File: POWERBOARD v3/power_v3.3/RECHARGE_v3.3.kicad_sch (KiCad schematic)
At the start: 27 parts, among them J1 B2B_PH_K_S, J2 USB_C_Receptacle_USB2.0_16P, J3 R14 - 103AT-2, U1 USBLC6-2, U2 BQ25886RGE

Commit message: added footprints
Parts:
- removed CHAR/BATT1: CHAR/BATT, Connector_PinHeader_2.00mm:PinHeader_1x02_P2.00mm_Vertical, symbol Connector_Generic:Conn_01x02
- removed J1: B2B_PH_K_S, Connector_JST:JST_PH_B2B-PH-K_1x02_P2.00mm_Vertical, symbol Connector_Generic:Conn_01x02
- removed J2: USB_C_Receptacle_USB2.0_16P, symbol Connector:USB_C_Receptacle_USB2.0_16P
- removed J3: R14 - 103AT-2, symbol Connector_Generic:Conn_01x02
- added BAT1: TestPoint, TestPoint:TestPoint_Keystone_5000-5004_Miniature, symbol Connector:TestPoint
- added C13: 22n, Capacitor_SMD:C_0201_0603Metric, symbol Device:C
- added J1: 2053380003, footprintsusbc:CONN_2053380000-SD_03_MOL, symbol 2026-10-06_11-57-55:2053380003
- added J2: UJ20-C-H-G-SMT-1-P16-TR, UJ20-C-H-G-SMT-1-P16-TR:SAMESKY_UJ20-C-H-G-SMT-1-P16-TR, symbol UJ20-C-H-G-SMT-1-P16-TR:UJ20-C-H-G-SMT-1-P16-TR
- C1: value 30u -> 22u
- C2: value 47n -> 22n; footprint Capacitor_SMD:C_1206_3216Metric -> Capacitor_SMD:C_0201_0603Metric
- C4, C8, C9: footprint (none) -> Capacitor_SMD:C_1206_3216Metric
- C6, C7: footprint Capacitor_SMD:C_0805_2012Metric -> Capacitor_SMD:C_1206_3216Metric
- D1, D2: footprint LED_SMD:LED_0805_2012Metric -> LED_SMD:LED_0603_1608Metric
- L1: footprint (none) -> 74438336010:INDC3030X200N
- R1: value 3.9k -> 6.2k; footprint Resistor_SMD:R_0805_2012Metric -> Resistor_SMD:R_0603_1608Metric
- R2, R4, R6, R7, R8, R9: footprint Resistor_SMD:R_0805_2012Metric -> Resistor_SMD:R_0603_1608Metric
- R3, R5: footprint (none) -> Resistor_SMD:R_0603_1608Metric
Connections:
- net BATTERY VOLTAGE: now also C8.1, U2.13 (BAT), U2.14 (BAT), BAT1.1, J1.3
- net BTST: now also C13.2
- net CC1: now also J2.A5 (CC1)
- net CC2: now also J2.B5 (CC2)
- net GND: now also J1.1, J2.A1_B12 (GND), J2.B1_A12 (GND__1), J2.SH1 (SHIELD), J2.SH2 (SHIELD__1), J2.SH3 (SHIELD__2), J2.SH4 (SHIELD__3); no longer U1.2 (GND)
- net SW: now also C13.1
- net VBUS: now also J2.A4_B9 (VBUS), J2.B4_A9 (VBUS__1)
- net at U1.1 (I/O1): now also J2.A6 (DP1), J2.B6 (DP2)
- net at U1.3 (I/O2): now also J2.A7 (DN1), J2.B7 (DN2)
- net TS renamed NTC
- net NTC: now also J1.2
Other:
- moved on the sheet: C2, C8, C9, D1, D2, R6, R7, R8, R9, U1, U2

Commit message: finished footprint assignment, added on-off general switch
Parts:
- J2: footprint UJ20-C-H-G-SMT-1-P16-TR:SAMESKY_UJ20-C-H-G-SMT-1-P16-TR -> UJ20_C_H_G_SMT_1_P16_TR:SAMESKY_UJ20-C-H-G-SMT-1-P16-TR
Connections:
- net GND: now also U1.2 (GND)
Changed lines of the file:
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@@
+	(wire
+		(pts
+			(xy 67.31 185.42) (xy 77.47 185.42)
+		)
+		(stroke
+			(width 0)
+			(type default)
+		)
+	)
 	(wire
 		(pts
@@
 	(wire
 		(pts
+			(xy 77.47 151.13) (xy 77.47 185.42)
+		)
+		(stroke
+			(width 0)
+			(type default)
+		)
+	)
+	(wire
+		(pts
 			(xy 33.02 43.18) (xy 33.02 36.83)
 		)
@@
 		(pts
 			(xy 59.69 36.83) (xy 52.07 36.83)
-		)
-		(stroke
-			(width 0)
-			(type default)
-		)
-	)
-	(wire
-		(pts
-			(xy 77.47 151.13) (xy 77.47 177.8)
 		)
 		(stroke
@@
 			)
 		)
-		(property "Footprint" "UJ20-C-H-G-SMT-1-P16-TR:SAMESKY_UJ20-C-H-G-SMT-1-P16-TR"
+		(property "Footprint" "UJ20_C_H_G_SMT_1_P16_TR:SAMESKY_UJ20-C-H-G-SMT-1-P16-TR"
 			(at 45.72 152.4 0)
 			(hide yes)

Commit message: (nearly) finished schematic and layout, beginning routing (hooooooly)
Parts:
- removed C9: 22u, Capacitor_SMD:C_1206_3216Metric, symbol Device:C
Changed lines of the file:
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@@
 	)
 	(junction
+		(at 209.55 46.99)
+		(diameter 0)
+		(color 0 0 0 0)
+	)
+	(junction
 		(at 238.76 133.35)
 		(diameter 0)
@@
 	)
 	(junction
-		(at 224.79 119.38)
-		(diameter 0)
-		(color 0 0 0 0)
-	)
-	(junction
 		(at 60.96 147.32)
 		(diameter 0)
@@
 	)
 	(junction
-		(at 209.55 46.99)
-		(diameter 0)
-		(color 0 0 0 0)
-	)
-	(junction
 		(at 67.31 177.8)
 		(diameter 0)
@@
 	(wire
 		(pts
+			(xy 83.82 101.6) (xy 83.82 107.95)
+		)
+		(stroke
+			(width 0)
+			(type default)
+		)
+	)
+	(wire
+		(pts
 			(xy 67.31 177.8) (xy 67.31 180.34)
 		)
@@
 	(wire
 		(pts
-			(xy 209.55 46.99) (xy 217.17 46.99)
+			(xy 33.02 50.8) (xy 33.02 54.61)
 		)
 		(stroke
@@
 	(wire
 		(pts
-			(xy 33.02 50.8) (xy 33.02 54.61)
+			(xy 237.49 107.95) (xy 229.87 107.95)
 		)
 		(stroke
@@
 	(wire
 		(pts
-			(xy 237.49 107.95) (xy 229.87 107.95)
+			(xy 209.55 46.99) (xy 217.17 46.99)
 		)
 		(stroke
@@
 	(wire
 		(pts
-			(xy 213.36 119.38) (xy 213.36 130.81)
-		)
-		(stroke
-			(width 0)
-			(type default)
-		)
-	)
-	(wire
-		(pts
 			(xy 49.53 110.49) (xy 78.74 110.49)
 		)
@@
 	(wire
 		(pts
-			(xy 224.79 119.38) (xy 233.68 119.38)
-		)
-		(stroke
-			(width 0)
-			(type default)
-		)
-	)
-	(wire
-		(pts
 			(xy 81.28 57.15) (xy 91.44 57.15)
 		)
@@
 	(wire
 		(pts
-			(xy 213.36 130.81) (xy 193.04 130.81)
+			(xy 193.04 130.81) (xy 215.9 130.81)
 		)
 		(stroke
@@
 	(wire
 		(pts
-			(xy 49.53 107.95) (xy 78.74 107.95)
-		)
-		(stroke
-			(width 0)
-			(type default)
-		)
-	)
-	(wire
-		(pts
 			(xy 58.42 142.24) (xy 60.96 142.24)
 		)
@@
 	(wire
 		(pts
+			(xy 83.82 107.95) (xy 49.53 107.95)
+		)
+		(stroke
+			(width 0)
+			(type default)
+		)
+	)
+	(wire
+		(pts
 			(xy 60.96 149.86) (xy 60.96 147.32)
 		)
@@
 	(wire
 		(pts
-			(xy 213.36 119.38) (xy 224.79 119.38)
-		)
-		(stroke
-			(width 0)
-			(type default)
-		)
-	)
-	(wire
-		(pts
 			(xy 237.49 101.6) (xy 237.49 104.14)
 		)
@@
 		)
 	)
-	(label "TS"
-		(at 203.2 143.51 180)
-		(effects
-			(font
-				(size 1.27 1.27)
-			)
-			(justify right bottom)
-		)
-	)
 	(label "SW"
 		(at 200.66 120.65 0)
@@
 		)
 	)
-	(label "NTC"
-		(at 78.74 107.95 180)
-		(effects
-			(font
-				(size 1.27 1.27)
-			)
-			(justify right bottom)
-		)
-	)
 	(label "D-"
 		(at 162.56 115.57 0)
@@
 		)
 	)
-	(label "NTC"
-		(at 217.17 46.99 0)
-		(effects
-			(font
-				(size 1.27 1.27)
-			)
-			(justify left bottom)
-		)
-	)
 	(label "ILIM"
 		(at 162.56 143.51 0)
@@
 		)
 	)
-	(label "TS"
+	(global_label "TS"
+		(shape input)
+		(at 203.2 143.51 0)
+		(fields_autoplaced yes)
+		(effects
+			(font
+				(size 1.27 1.27)
+			)
+			(justify left)
+		)
+		(property "Intersheetrefs" "${INTERSHEET_REFS}"
+			(at 208.3623 143.51 0)
+			(hide yes)
+			(show_name no)
+			(do_not_autoplace no)
+			(effects
+				(font
+					(size 1.27 1.27)
+				)
+				(justify left)
+			)
+		)
+	)
+	(global_label "NTC"
+		(shape bidirectional)
+		(at 217.17 46.99 0)
+		(fields_autoplaced yes)
+		(effects
+			(font
+				(size 1.27 1.27)
+			)
+			(justify left)
+		)
+		(property "Intersheetrefs" "${INTERSHEET_REFS}"
+			(at 224.8346 46.99 0)
+			(hide yes)
+			(show_name no)
+			(do_not_autoplace no)
+			(effects
+				(font
+					(size 1.27 1.27)
+				)
+				(justify left)
+			)
+		)
+	)
+	(global_label "TS"
+		(shape input)
 		(at 209.55 44.45 90)
+		(fields_autoplaced yes)
 		(effects
 			(font
 				(size 1.27 1.27)
 			)
-			(justify left bottom)
+			(justify left)
+		)
+		(property "Intersheetrefs" "${INTERSHEET_REFS}"
+			(at 209.55 39.2877 90)
+			(hide yes)
+			(show_name no)
+			(do_not_autoplace no)
+			(effects
+				(font
+					(size 1.27 1.27)
+				)
+				(justify left)
+			)
+		)
+	)
+	(global_label "NTC"
+		(shape bidirectional)
+		(at 83.82 101.6 90)
+		(fields_autoplaced yes)
+		(effects
+			(font
+				(size 1.27 1.27)
+			)
+			(justify left)
+		)
+		(property "Intersheetrefs" "${INTERSHEET_REFS}"
+			(at 83.82 93.9354 90)
+			(hide yes)
+			(show_name no)
+			(do_not_autoplace no)
+			(effects
+				(font
+					(size 1.27 1.27)
+				)
+				(justify left)
+			)
 		)
 	)
 	(hierarchical_label "SYS"
 		(shape output)
-		(at 233.68 119.38 0)
+		(at 215.9 130.81 0)
 		(effects
 			(font
@@
 	)
 	(symbol
-		(lib_id "power:GND")
-		(at 224.79 127 0)
-		(unit 1)
-		(body_style 1)
-		(exclude_from_sim no)
-		(in_bom yes)
-		(on_board yes)
-		(in_pos_files yes)
-		(dnp no)
-		(fields_autoplaced yes)
-		(property "Reference" "#PWR015"
-			(at 224.79 133.35 0)
-			(hide yes)
-			(show_name no)
-			(do_not_autoplace no)
-			(effects
-				(font
-					(size 1.27 1.27)
-				)
-			)
-		)
-		(property "Value" "GND"
-			(at 224.79 132.08 0)
-			(show_name no)
-			(do_not_autoplace no)
-			(effects
-				(font
-					(size 1.27 1.27)
-				)
-			)
-		)
-		(property "Footprint" ""
-			(at 224.79 127 0)
-			(hide yes)
-			(show_name no)
-			(do_not_autoplace no)
-			(effects
-				(font
-					(size 1.27 1.27)
-				)
-			)
-		)
-		(property "Datasheet" ""
-			(at 224.79 127 0)
-			(hide yes)
-			(show_name no)
-			(do_not_autoplace no)
-			(effects
-				(font
-					(size 1.27 1.27)
-				)
-			)
-		)
-		(property "Description" "Power symbol creates a global label with name \"GND\" , ground"
-			(at 224.79 127 0)
-			(hide yes)
-			(show_name no)
-			(do_not_autoplace no)
-			(effects
-				(font
-					(size 1.27 1.27)
-				)
-			)
-		)
-		(pin "1"
-		)
-		(instances
-			(project "power_v3.3"
-				(path "/432bcdcf-747a-4fa0-b87b-096f44260199/ef6b3a2b-31e3-4ffb-9457-e6034dbdb4b5"
-					(reference "#PWR015")
-					(unit 1)
-				)
-			)
-		)
-	)
-	(symbol
 		(lib_id "Device:C")
 		(at 54.61 59.69 0)
@@
 					(unit 1)
 				)
-			)
-		)
-	)
-	(symbol
-		(lib_id "Device:C")
-		(at 224.79 123.19 0)
-		(unit 1)
-		(body_style 1)
-		(exclude_from_sim no)
-		(in_bom yes)
-		(on_board yes)
-		(in_pos_files yes)
-		(dnp no)
-		(fields_autoplaced yes)
-		(property "Reference" "C9"
-			(at 228.6 121.9199 0)
-			(show_name no)
-			(do_not_autoplace no)
-			(effects
-				(font
-					(size 1.27 1.27)
-				)
-				(justify left)
-			)
-		)
-		(property "Value" "22u"
-			(at 228.6 124.4599 0)
-			(show_name no)
-			(do_not_autoplace no)
-			(effects
-				(font
-					(size 1.27 1.27)
-				)
-				(justify left)
-			)
-		)
-		(property "Footprint" "Capacitor_SMD:C_1206_3216Metric"
-			(at 225.7552 127 0)
-			(hide yes)
-			(show_name no)
-			(do_not_autoplace no)
-			(effects
-				(font
-					(size 1.27 1.27)
-				)
-			)
-		)
-		(property "Datasheet" ""
-			(at 224.79 123.19 0)
-			(hide yes)
-			(show_name no)
-			(do_not_autoplace no)
-			(effects
-				(font
-					(size 1.27 1.27)
-				)
-			)
-		)
-		(property "Description" "Unpolarized capacitor"
-			(at 224.79 123.19 0)
-			(hide yes)
-			(show_name no)
-			(do_not_autoplace no)
-			(effects
-				(font
-					(size 1.27 1.27)
-				)
-			)
-		)
-		(pin "1"
-		)
-		(pin "2"
-		)
-		(instances
-			(project "power_v3.3"
-				(path "/432bcdcf-747a-4fa0-b87b-096f44260199/ef6b3a2b-31e3-4ffb-9457-e6034dbdb4b5"
-					(reference "C9")
-					(unit 1)
-				)

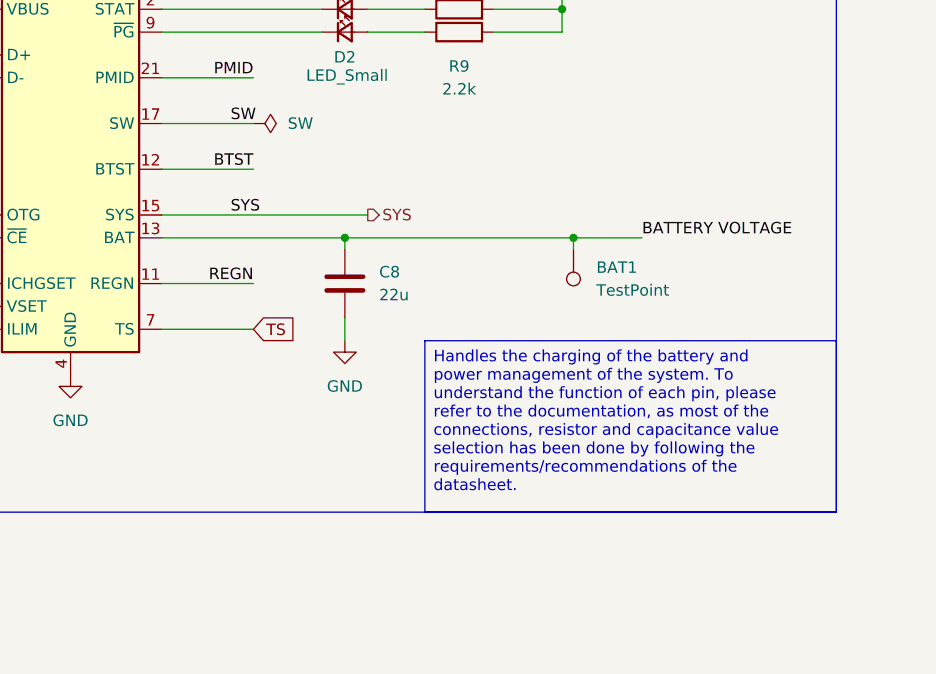
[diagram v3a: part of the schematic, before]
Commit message: updated routing, added mounting holes
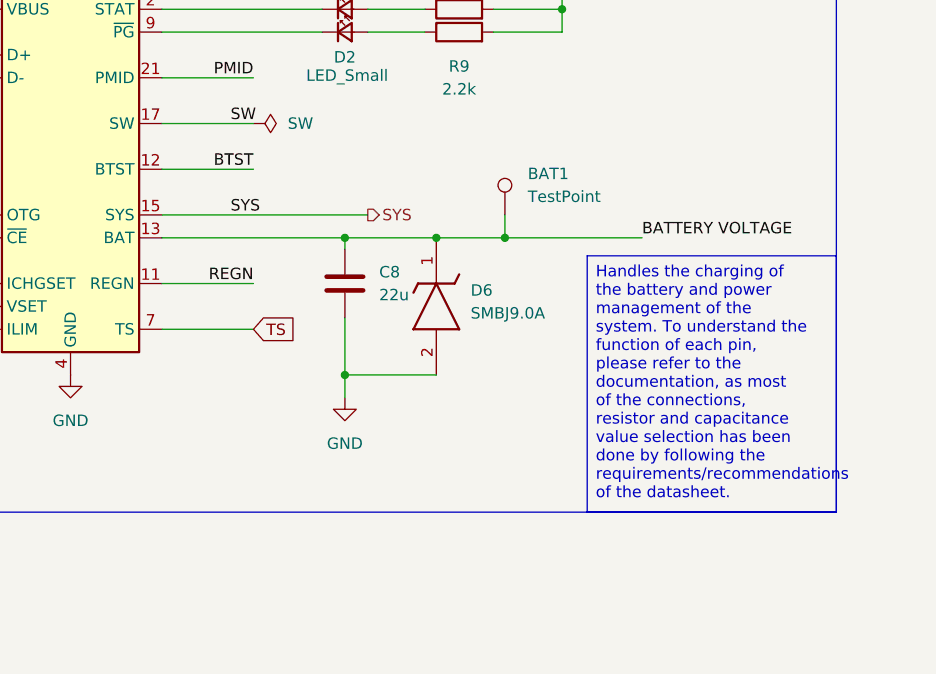
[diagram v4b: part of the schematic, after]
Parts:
- added D6: SMBJ9.0A, SMBJ9.0A:DIOM5436X261N, symbol SMBJ9_0A:SMBJ9.0A
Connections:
- net BATTERY VOLTAGE: now also D6.1 (K)
- net GND: now also D6.2 (A)
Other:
- moved on the sheet: BAT1
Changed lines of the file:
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@@
 	(text_box "Handles the charging of the battery and power management of the system. To understand the function of each pin, please refer to the documentation, as most of the connections, resistor and capacitance value selection has been done by following the requirements/recommendations of the datasheet."
 		(exclude_from_sim no)
-		(at 222.25 144.7799 0)
-		(size 45.72 19.0501)
+		(at 240.284 135.3462 0)
+		(size 27.686 28.4838)
 		(margins 0.9525 0.9525 0.9525 0.9525)
 		(stroke
@@
 	)
 	(junction
-		(at 238.76 133.35)
+		(at 231.14 133.35)
 		(diameter 0)
 		(color 0 0 0 0)
@@
 	)
 	(junction
+		(at 223.52 133.35)
+		(diameter 0)
+		(color 0 0 0 0)
+	)
+	(junction
 		(at 67.31 180.34)
 		(diameter 0)
@@
 	)
 	(junction
+		(at 213.36 148.59)
+		(diameter 0)
+		(color 0 0 0 0)
+	)
+	(junction
 		(at 170.18 44.45)
 		(diameter 0)
@@
 	(wire
 		(pts
+			(xy 213.36 148.59) (xy 213.36 142.24)
+		)
+		(stroke
+			(width 0)
+			(type default)
+		)
+	)
+	(wire
+		(pts
 			(xy 60.96 132.08) (xy 77.47 132.08)
 		)
@@
 	(wire
 		(pts
-			(xy 213.36 144.78) (xy 213.36 142.24)
+			(xy 213.36 151.13) (xy 213.36 148.59)
 		)
 		(stroke
@@
 	(wire
 		(pts
-			(xy 193.04 133.35) (xy 238.76 133.35)
+			(xy 223.52 133.35) (xy 246.38 133.35)
+		)
+		(stroke
+			(width 0)
+			(type default)
+		)
+	)
+	(wire
+		(pts
+			(xy 193.04 133.35) (xy 223.52 133.35)
 		)
 		(stroke
@@
 	(wire
 		(pts
-			(xy 238.76 134.62) (xy 238.76 133.35)
+			(xy 231.14 130.81) (xy 231.14 133.35)
 		)
 		(stroke
@@
 	(wire
 		(pts
-			(xy 213.36 134.62) (xy 213.36 133.35)
+			(xy 213.36 148.59) (xy 223.52 148.59)
 		)
 		(stroke
@@
 	(wire
 		(pts
-			(xy 43.18 64.77) (xy 43.18 63.5)
+			(xy 213.36 134.62) (xy 213.36 133.35)
 		)
 		(stroke
@@
 	(wire
 		(pts
-			(xy 238.76 133.35) (xy 246.38 133.35)
+			(xy 43.18 64.77) (xy 43.18 63.5)
 		)
 		(stroke
@@
 	)
 	(symbol
+		(lib_id "SMBJ9_0A:SMBJ9.0A")
+		(at 223.52 133.35 270)
+		(unit 1)
+		(body_style 1)
+		(exclude_from_sim no)
+		(in_bom yes)
+		(on_board yes)
+		(in_pos_files yes)
+		(dnp no)
+		(fields_autoplaced yes)
+		(property "Reference" "D6"
+			(at 227.33 139.1919 90)
+			(show_name no)
+			(do_not_autoplace no)
+			(effects
+				(font
+					(size 1.27 1.27)
+				)
+				(justify left)
+			)
+		)
+		(property "Value" "SMBJ9.0A"
+			(at 227.33 141.7319 90)
+			(show_name no)
+			(do_not_autoplace no)
+			(effects
+				(font
+					(size 1.27 1.27)
+				)
+				(justify left)
+			)
+		)
+		(property "Footprint" "SMBJ9.0A:DIOM5436X261N"
+			(at 129.87 143.51 0)
+			(hide yes)
+			(show_name no)
+			(do_not_autoplace no)
+			(effects
+				(font
+					(size 1.27 1.27)
+				)
+				(justify left bottom)
+			)
+		)
+		(property "Datasheet" "https://www.semtech.com/products/circuit-protection/esd-protection/smbj9.0a"
+			(at 29.87 143.51 0)
+			(hide yes)
+			(show_name no)
+			(do_not_autoplace no)
+			(effects
+				(font
+					(size 1.27 1.27)
+				)
+				(justify left bottom)
+			)
+		)
+		(property "Description" "1-Line ESD Protection"
+			(at 223.52 133.35 0)
+			(hide yes)
+			(show_name no)
+			(do_not_autoplace no)
+			(effects
+				(font
+					(size 1.27 1.27)
+				)
+			)
+		)
+		(property "Height" "2.61"
+			(at -170.13 143.51 0)
+			(hide yes)
+			(show_name no)
+			(do_not_autoplace no)
+			(effects
+				(font
+					(size 1.27 1.27)
+				)
+				(justify left bottom)
+			)
+		)
+		(property "Mouser Part Number" ""
+			(at -270.13 143.51 0)
+			(hide yes)
+			(show_name no)
+			(do_not_autoplace no)
+			(effects
+				(font
+					(size 1.27 1.27)
+				)
+				(justify left bottom)
+			)
+		)
+		(property "Mouser Price/Stock" ""
+			(at -370.13 143.51 0)
+			(hide yes)
+			(show_name no)
+			(do_not_autoplace no)
+			(effects
+				(font
+					(size 1.27 1.27)
+				)
+				(justify left bottom)
+			)
+		)
+		(property "Manufacturer_Name" "SEMTECH"
+			(at -470.13 143.51 0)
+			(hide yes)
+			(show_name no)
+			(do_not_autoplace no)
+			(effects
+				(font
+					(size 1.27 1.27)
+				)
+				(justify left bottom)
+			)
+		)
+		(property "Manufacturer_Part_Number" "SMBJ9.0A"
+			(at -570.13 143.51 0)
+			(hide yes)
+			(show_name no)
+			(do_not_autoplace no)
+			(effects
+				(font
+					(size 1.27 1.27)
+				)
+				(justify left bottom)
+			)
+		)
+		(pin "1"
+		)
+		(pin "2"
+		)
+		(instances
+			(project "power_v3.3"
+				(path "/432bcdcf-747a-4fa0-b87b-096f44260199/ef6b3a2b-31e3-4ffb-9457-e6034dbdb4b5"
+					(reference "D6")
+					(unit 1)
+				)
+			)
+		)
+	)
+	(symbol
 		(lib_id "power:PWR_FLAG")
 		(at 237.49 104.14 270)
@@
 	(symbol
 		(lib_id "Connector:TestPoint")
-		(at 238.76 134.62 180)
+		(at 231.14 130.81 0)
 		(unit 1)
 		(body_style 1)
@@
 		(fields_autoplaced yes)
 		(property "Reference" "BAT1"
-			(at 241.3 136.6519 0)
+			(at 233.68 126.2379 0)
 			(show_name no)
 			(do_not_autoplace no)
@@
 					(size 1.27 1.27)
 				)
-				(justify right)
+				(justify left)
 			)
 		)
 		(property "Value" "TestPoint"
-			(at 241.3 139.1919 0)
+			(at 233.68 128.7779 0)
 			(show_name no)
 			(do_not_autoplace no)
@@
 					(size 1.27 1.27)
 				)
-				(justify right)
+				(justify left)
 			)
 		)
 		(property "Footprint" "TestPoint:TestPoint_Keystone_5000-5004_Miniature"
-			(at 233.68 134.62 0)
+			(at 236.22 130.81 0)
 			(hide yes)
 			(show_name no)
@@
 		)
 		(property "Datasheet" ""
-			(at 233.68 134.62 0)
+			(at 236.22 130.81 0)
 			(hide yes)
 			(show_name no)
@@
 		)
 		(property "Description" "test point"
-			(at 238.76 134.62 0)
+			(at 231.14 130.81 0)
 			(hide yes)
 			(show_name no)
@@
 	(symbol
 		(lib_id "power:GND")
-		(at 213.36 144.78 0)
+		(at 213.36 151.13 0)
 		(unit 1)
 		(body_style 1)
@@
 		(fields_autoplaced yes)
 		(property "Reference" "#PWR013"
-			(at 213.36 151.13 0)
+			(at 213.36 157.48 0)
 			(hide yes)
 			(show_name no)
@@
 		)
 		(property "Value" "GND"
-			(at 213.36 149.86 0)
+			(at 213.36 156.21 0)
 			(show_name no)
 			(do_not_autoplace no)
@@
 		)
 		(property "Footprint" ""
-			(at 213.36 144.78 0)
+			(at 213.36 151.13 0)
 			(hide yes)
 			(show_name no)
@@
 		)
 		(property "Datasheet" ""
-			(at 213.36 144.78 0)
+			(at 213.36 151.13 0)
 			(hide yes)
 			(show_name no)
@@
 		)
 		(property "Description" "Power symbol creates a global label with name \"GND\" , ground"
-			(at 213.36 144.78 0)
+			(at 213.36 151.13 0)
 			(hide yes)
 			(show_name no)
